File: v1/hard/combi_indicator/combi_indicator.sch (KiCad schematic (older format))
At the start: 35 parts, among them J1 Conn_01x04_Male, U1 HT7991

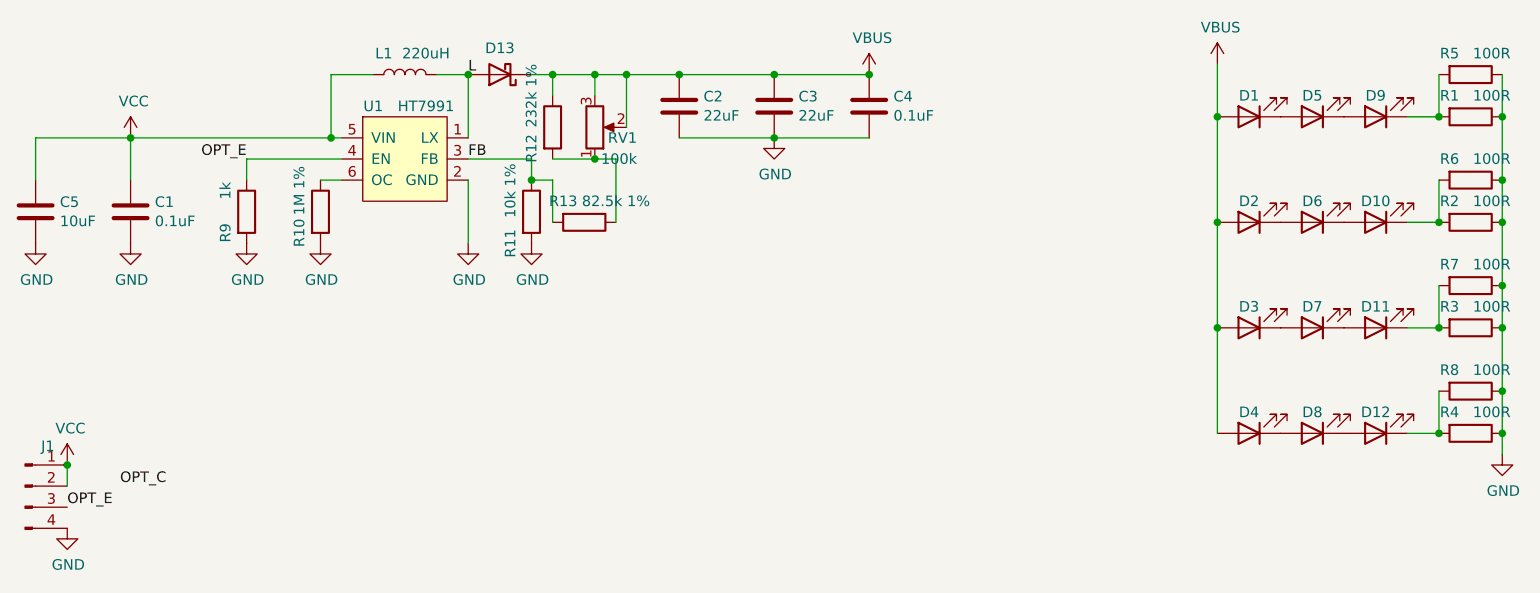
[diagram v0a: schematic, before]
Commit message: Moved connectors location to 2.54 grid for better compartibility with predrilled prototyping boards.
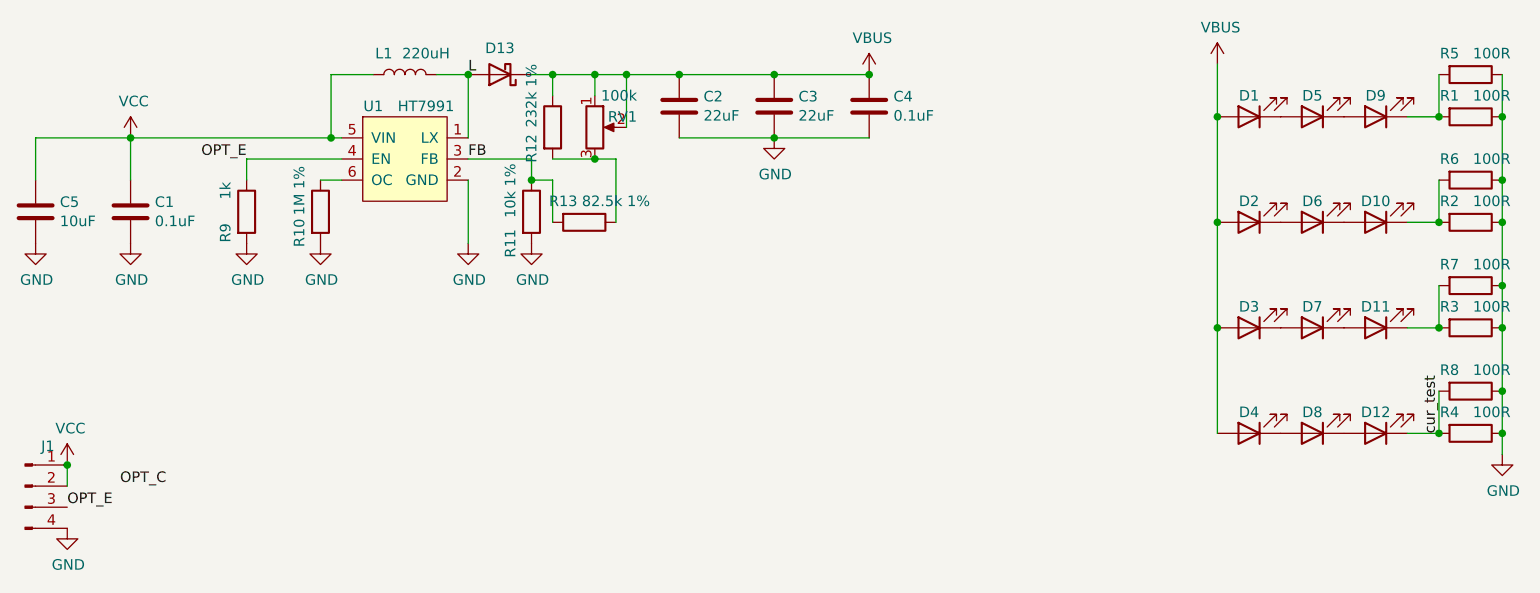
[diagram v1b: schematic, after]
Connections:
- net VBUS: now also RV1.1; no longer RV1.3
- net cur_test: now reaches D12.1 (K), R4.2, R8.2
- net at R12.2, R13.1: now also RV1.3; no longer RV1.1
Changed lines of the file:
@@
 F 3 "~" H 3600 1300 50  0001 C CNN
 	1    3600 1300
-	1    0    0    1
+	1    0    0    -1
 $EndComp
 Wire Wire Line
@@
 	3700 1450 3700 1750
 Connection ~ 3600 1450
+Text Label 7600 2750 1    50   ~ 0
+cur_test
 $EndSCHEMATC

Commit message: Finished "combi indicator" - indicator board for combi button, v0.1. Added table with resistor values for LED of different color. Also provided spreadsheet with all formulas.
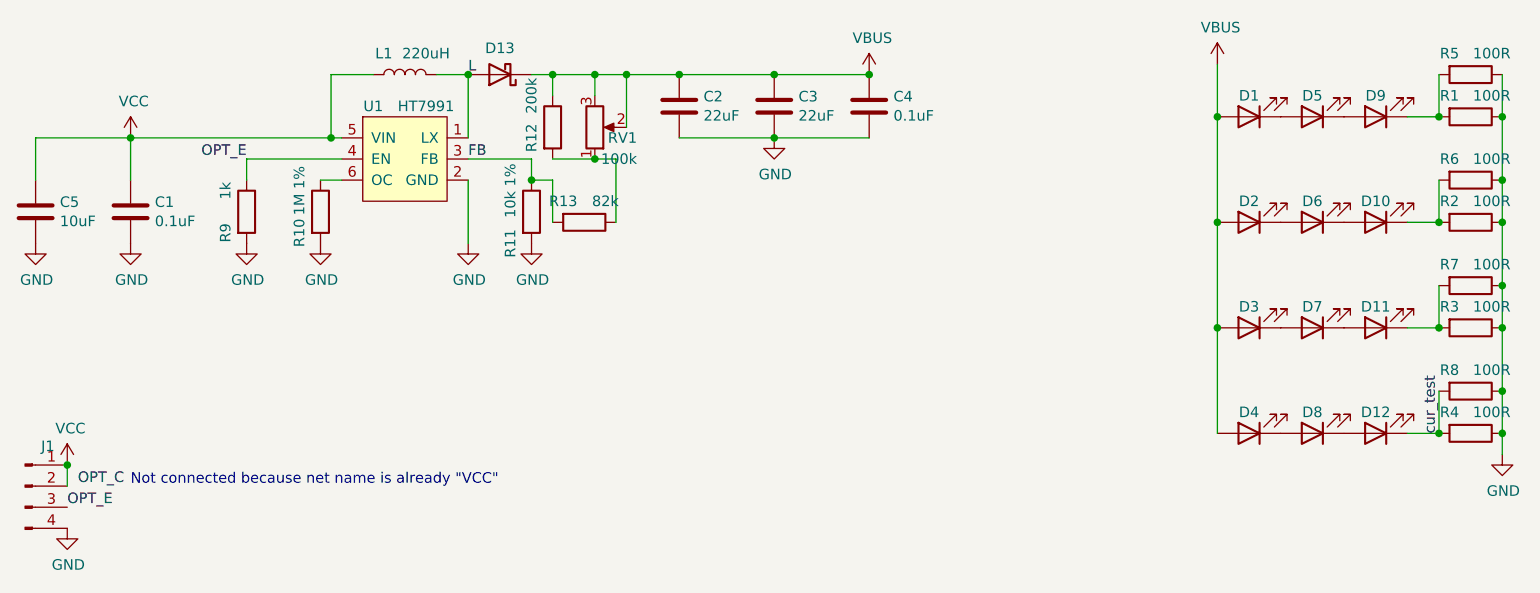
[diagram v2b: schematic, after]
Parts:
- R12: value 232k 1% -> 200k
- R13: value 82.5k 1% -> 82k
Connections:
- net VBUS: now also RV1.3; no longer RV1.1
- net at R12.2, R13.1: now also RV1.1; no longer RV1.3
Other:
- note added: "Not connected because net name is already "VCC""
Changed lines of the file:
@@
 	1    0    0    -1
 $EndComp
-Text Label 1350 3000 0    50   ~ 0
+Text Label 1150 3000 0    50   ~ 0
 OPT_C
 Text Label 1100 3100 0    50   ~ 0
@@
 U 1 1 607D397B
 P 3400 1300
-F 0 "R12" V 3300 1200 50  0000 C CNN
-F 1 "232k 1%" V 3300 1450 50  0000 C CNN
+F 0 "R12" V 3300 1250 50  0000 C CNN
+F 1 "200k" V 3300 1450 50  0000 C CNN
 F 2 "Resistor_SMD:R_0805_2012Metric_Pad1.15x1.40mm_HandSolder" V 3330 1300 50  0001 C CNN
 F 3 "~" H 3400 1300 50  0001 C CNN
@@
 F 3 "~" H 3600 1300 50  0001 C CNN
 	1    3600 1300
-	1    0    0    -1
+	1    0    0    1
 $EndComp
 Wire Wire Line
@@
 P 3550 1750
 F 0 "R13" V 3450 1650 50  0000 C CNN
-F 1 "82.5k 1%" V 3450 1900 50  0000 C CNN
+F 1 "82k" V 3450 1850 50  0000 C CNN
 F 2 "Resistor_SMD:R_0805_2012Metric_Pad1.15x1.40mm_HandSolder" V 3480 1750 50  0001 C CNN
 F 3 "~" H 3550 1750 50  0001 C CNN
@@
 Text Label 7600 2750 1    50   ~ 0
 cur_test
+Text Notes 1400 3000 0    50   ~ 0
+Not connected because net name is already "VCC"
 $EndSCHEMATC
